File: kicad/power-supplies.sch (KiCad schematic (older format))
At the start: 22 parts, among them U3 MCP1603, U4 MIC2776L, U5 MIC5501-XYM5

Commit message: Finished initial part selection, built footprints
I'm not sure about my footprint selection for the expansion headers,
even though it is just a 0.1" header I want to be fairly exact about the
length the pins stick out and how close the female header is to the
edge, so that I can get a good distance between the two boards.
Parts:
- C14, C18: footprint (none) -> Capacitors_SMD:C_0805; Part No. (none) -> 1276-6464-1-ND
- C15, C17, C20, C21: footprint (none) -> Capacitors_SMD:C_0603; Part No. (none) -> 1276-6524-1-ND
- C16, C19: footprint (none) -> Capacitors_SMD:C_0402; Part No. (none) -> 1276-1043-1-ND
- L2: footprint (none) -> midi-fader:Wurth_TPC_3816; Part No. (none) -> 732-1008-1-ND
- R14: footprint (none) -> Resistors_SMD:R_0805
- R15, R16, R18, R19, R20, R21, R22, R23: footprint (none) -> Resistors_SMD:R_0402
- U3: footprint (none) -> TO_SOT_Packages_SMD:TSOT-23-5
- U4, U5: footprint (none) -> TO_SOT_Packages_SMD:SOT-23-5
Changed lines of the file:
@@
 LIBS:valves
 LIBS:midi-fader
+LIBS:midi-fader-cache
 EELAYER 25 0
 EELAYER END
@@
 F 0 "U3" H 7450 2050 60  0000 C CNN
 F 1 "MCP1603" H 7300 2550 60  0000 C CNN
-F 2 "" H 7300 1900 60  0001 C CNN
+F 2 "TO_SOT_Packages_SMD:TSOT-23-5" H 7300 1900 60  0001 C CNN
 F 3 "" H 7300 1900 60  0001 C CNN
 F 4 "MCP1603T-330I/OSCT-ND" H 7300 2650 60  0001 C CNN "Part No."
@@
 F 0 "U5" H 3100 3650 60  0000 C CNN
 F 1 "MIC5501-XYM5" H 2900 4150 60  0000 C CNN
-F 2 "" H 2900 3800 60  0001 C CNN
+F 2 "TO_SOT_Packages_SMD:SOT-23-5" H 2900 3800 60  0001 C CNN
 F 3 "" H 2900 3800 60  0001 C CNN
 F 4 "576-4764-1-ND" H 2900 4250 60  0001 C CNN "Part No."
@@
 F 0 "L2" V 8100 2200 50  0000 C CNN
 F 1 "4.7u" V 8225 2200 50  0000 C CNN
-F 2 "" H 8150 2200 50  0001 C CNN
+F 2 "midi-fader:Wurth_TPC_3816" H 8150 2200 50  0001 C CNN
 F 3 "" H 8150 2200 50  0001 C CNN
+F 4 "732-1008-1-ND" H 8150 2200 60  0001 C CNN "Part No."
 	1    8150 2200
 	0    -1   -1   0
@@
 F 0 "C18" H 8975 2750 50  0000 L CNN
 F 1 "4.7u" H 8975 2550 50  0000 L CNN
-F 2 "" H 8988 2500 50  0001 C CNN
+F 2 "Capacitors_SMD:C_0805" H 8988 2500 50  0001 C CNN
 F 3 "" H 8950 2650 50  0001 C CNN
+F 4 "1276-6464-1-ND" H 8950 2650 60  0001 C CNN "Part No."
 	1    8950 2650
 	1    0    0    -1
 $EndComp
 $Comp
-L VBUS #PWR15
+L VBUS #PWR023
 U 1 1 5B3CF911
 P 1000 2100
-F 0 "#PWR15" H 1000 1950 50  0001 C CNN
+F 0 "#PWR023" H 1000 1950 50  0001 C CNN
 F 1 "VBUS" H 1000 2250 50  0000 C CNN
 F 2 "" H 1000 2100 50  0001 C CNN
@@
 F 0 "C14" H 1025 2550 50  0000 L CNN
 F 1 "4.7u" H 1025 2350 50  0000 L CNN
-F 2 "" H 1038 2300 50  0001 C CNN
+F 2 "Capacitors_SMD:C_0805" H 1038 2300 50  0001 C CNN
 F 3 "" H 1000 2450 50  0001 C CNN
+F 4 "1276-6464-1-ND" H 1000 2450 60  0001 C CNN "Part No."
 	1    1000 2450
 	1    0    0    -1
@@
 F 0 "C15" H 1325 2550 50  0000 L CNN
 F 1 "1u" H 1325 2350 50  0000 L CNN
-F 2 "" H 1338 2300 50  0001 C CNN
+F 2 "Capacitors_SMD:C_0603" H 1338 2300 50  0001 C CNN
 F 3 "" H 1300 2450 50  0001 C CNN
+F 4 "1276-6524-1-ND" H 1300 2450 60  0001 C CNN "Part No."
 	1    1300 2450
 	1    0    0    -1
@@
 F 0 "R15" V 2980 2450 50  0000 C CNN
 F 1 "10K" V 2900 2450 50  0000 C CNN
-F 2 "" V 2830 2450 50  0001 C CNN
+F 2 "Resistors_SMD:R_0402" V 2830 2450 50  0001 C CNN
 F 3 "" H 2900 2450 50  0001 C CNN
 	1    2900 2450
@@
 F 0 "R18" V 2980 2950 50  0000 C CNN
 F 1 "750" V 2900 2950 50  0000 C CNN
-F 2 "" V 2830 2950 50  0001 C CNN
+F 2 "Resistors_SMD:R_0402" V 2830 2950 50  0001 C CNN
 F 3 "" H 2900 2950 50  0001 C CNN
 	1    2900 2950
@@
 F 0 "R20" V 1980 3750 50  0000 C CNN
 F 1 "0" V 1900 3750 50  0000 C CNN
-F 2 "" V 1830 3750 50  0001 C CNN
+F 2 "Resistors_SMD:R_0402" V 1830 3750 50  0001 C CNN
 F 3 "" H 1900 3750 50  0001 C CNN
 	1    1900 3750
@@
 F 0 "R22" V 1980 4250 50  0000 C CNN
 F 1 "SPR" V 1900 4250 50  0000 C CNN
-F 2 "" V 1830 4250 50  0001 C CNN
+F 2 "Resistors_SMD:R_0402" V 1830 4250 50  0001 C CNN
 F 3 "" H 1900 4250 50  0001 C CNN
 	1    1900 4250
@@
 $EndComp
 $Comp
-L GND #PWR26
+L GND #PWR024
 U 1 1 5B3CFC0A
 P 1900 4600
-F 0 "#PWR26" H 1900 4350 50  0001 C CNN
+F 0 "#PWR024" H 1900 4350 50  0001 C CNN
 F 1 "GND" H 1900 4450 50  0000 C CNN
 F 2 "" H 1900 4600 50  0001 C CNN
@@
 F 0 "R14" V 1680 2450 50  0000 C CNN
 F 1 "1K" V 1600 2450 50  0000 C CNN
-F 2 "" V 1530 2450 50  0001 C CNN
+F 2 "Resistors_SMD:R_0805" V 1530 2450 50  0001 C CNN
 F 3 "" H 1600 2450 50  0001 C CNN
 	1    1600 2450
@@
 F 0 "U4" H 5650 2550 60  0000 C CNN
 F 1 "MIC2776L" H 5500 3050 60  0000 C CNN
-F 2 "" H 5500 2800 60  0001 C CNN
+F 2 "TO_SOT_Packages_SMD:SOT-23-5" H 5500 2800 60  0001 C CNN
 F 3 "" H 5500 2800 60  0001 C CNN
 F 4 "576-2686-1-ND" H 5500 3150 60  0001 C CNN "Part No."
@@
 $EndComp
 $Comp
-L GND #PWR18
+L GND #PWR025
 U 1 1 5B3D0BA6
 P 1000 2800
-F 0 "#PWR18" H 1000 2550 50  0001 C CNN
+F 0 "#PWR025" H 1000 2550 50  0001 C CNN
 F 1 "GND" H 1000 2650 50  0000 C CNN
 F 2 "" H 1000 2800 50  0001 C CNN
@@
 F 0 "C20" H 3575 4250 50  0000 L CNN
 F 1 "1u" H 3575 4050 50  0000 L CNN
-F 2 "" H 3588 4000 50  0001 C CNN
+F 2 "Capacitors_SMD:C_0603" H 3588 4000 50  0001 C CNN
 F 3 "" H 3550 4150 50  0001 C CNN
+F 4 "1276-6524-1-ND" H 3550 4150 60  0001 C CNN "Part No."
 	1    3550 4150
 	1    0    0    -1
@@
 F 0 "C21" H 3825 4250 50  0000 L CNN
 F 1 "1u" H 3825 4050 50  0000 L CNN
-F 2 "" H 3838 4000 50  0001 C CNN
+F 2 "Capacitors_SMD:C_0603" H 3838 4000 50  0001 C CNN
 F 3 "" H 3800 4150 50  0001 C CNN
+F 4 "1276-6524-1-ND" H 3800 4150 60  0001 C CNN "Part No."
 	1    3800 4150
 	1    0    0    -1
@@
 F 0 "C19" H 4525 3000 50  0000 L CNN
 F 1 "0.1u" H 4525 2800 50  0000 L CNN
-F 2 "" H 4538 2750 50  0001 C CNN
+F 2 "Capacitors_SMD:C_0402" H 4538 2750 50  0001 C CNN
 F 3 "" H 4500 2900 50  0001 C CNN
+F 4 "1276-1043-1-ND" H 4500 2900 60  0001 C CNN "Part No."
 	1    4500 2900
 	1    0    0    -1
 $EndComp
 $Comp
-L GND #PWR21
+L GND #PWR026
 U 1 1 5B3D1467
 P 4500 3150
-F 0 "#PWR21" H 4500 2900 50  0001 C CNN
+F 0 "#PWR026" H 4500 2900 50  0001 C CNN
 F 1 "GND" H 4500 3000 50  0000 C CNN
 F 2 "" H 4500 3150 50  0001 C CNN
@@
 F 0 "R21" V 4580 4050 50  0000 C CNN
 F 1 "10K" V 4500 4050 50  0000 C CNN
-F 2 "" V 4430 4050 50  0001 C CNN
+F 2 "Resistors_SMD:R_0402" V 4430 4050 50  0001 C CNN
 F 3 "" H 4500 4050 50  0001 C CNN
 	1    4500 4050
@@
 F 0 "R23" V 4580 4550 50  0000 C CNN
 F 1 "SPR" V 4500 4550 50  0000 C CNN
-F 2 "" V 4430 4550 50  0001 C CNN
+F 2 "Resistors_SMD:R_0402" V 4430 4550 50  0001 C CNN
 F 3 "" H 4500 4550 50  0001 C CNN
 	1    4500 4550
@@
 $EndComp
 $Comp
-L VDDA #PWR25
+L VDDA #PWR027
 U 1 1 5B3D1EBD
 P 3900 3700
-F 0 "#PWR25" H 3900 3550 50  0001 C CNN
+F 0 "#PWR027" H 3900 3550 50  0001 C CNN
 F 1 "VDDA" H 3900 3850 50  0000 C CNN
 F 2 "" H 3900 3700 50  0001 C CNN
@@
 $EndComp
 $Comp
-L GND #PWR27
+L GND #PWR028
 U 1 1 5B3D212E
 P 4500 4800
-F 0 "#PWR27" H 4500 4550 50  0001 C CNN
+F 0 "#PWR028" H 4500 4550 50  0001 C CNN
 F 1 "GND" H 4500 4650 50  0000 C CNN
 F 2 "" H 4500 4800 50  0001 C CNN
@@
 $EndComp
 $Comp
-L GND #PWR22
+L GND #PWR029
 U 1 1 5B3D21E1
 P 2900 3200
-F 0 "#PWR22" H 2900 2950 50  0001 C CNN
+F 0 "#PWR029" H 2900 2950 50  0001 C CNN
 F 1 "GND" H 2900 3050 50  0000 C CNN
 F 2 "" H 2900 3200 50  0001 C CNN
@@
 $EndComp
 $Comp
-L GND #PWR23
+L GND #PWR030
 U 1 1 5B3D2387
 P 5500 3200
-F 0 "#PWR23" H 5500 2950 50  0001 C CNN
+F 0 "#PWR030" H 5500 2950 50  0001 C CNN
 F 1 "GND" H 5500 3050 50  0000 C CNN
 F 2 "" H 5500 3200 50  0001 C CNN
@@
 F 0 "C16" H 8475 2750 50  0000 L CNN
 F 1 "0.1u" H 8475 2550 50  0000 L CNN
-F 2 "" H 8488 2500 50  0001 C CNN
+F 2 "Capacitors_SMD:C_0402" H 8488 2500 50  0001 C CNN
 F 3 "" H 8450 2650 50  0001 C CNN
+F 4 "1276-1043-1-ND" H 8450 2650 60  0001 C CNN "Part No."
 	1    8450 2650
 	1    0    0    -1
@@
 F 0 "C17" H 8725 2750 50  0000 L CNN
 F 1 "1u" H 8725 2550 50  0000 L CNN
-F 2 "" H 8738 2500 50  0001 C CNN
+F 2 "Capacitors_SMD:C_0603" H 8738 2500 50  0001 C CNN
 F 3 "" H 8700 2650 50  0001 C CNN
+F 4 "1276-6524-1-ND" H 8700 2650 60  0001 C CNN "Part No."
 	1    8700 2650
 	1    0    0    -1
@@
 15mA\n50mW\nRC=1.47ms
 $Comp
-L GND #PWR20
+L GND #PWR031
 U 1 1 5B3D2E2E
 P 8450 3000
-F 0 "#PWR20" H 8450 2750 50  0001 C CNN
+F 0 "#PWR031" H 8450 2750 50  0001 C CNN
 F 1 "GND" H 8450 2850 50  0000 C CNN
 F 2 "" H 8450 3000 50  0001 C CNN
@@
 F 0 "R16" V 6480 2450 50  0000 C CNN
 F 1 "SPR" V 6400 2450 50  0000 C CNN
-F 2 "" V 6330 2450 50  0001 C CNN
+F 2 "Resistors_SMD:R_0402" V 6330 2450 50  0001 C CNN
 F 3 "" H 6400 2450 50  0001 C CNN
 	1    6400 2450
@@
 F 0 "R19" V 6480 3050 50  0000 C CNN
 F 1 "SPR" V 6400 3050 50  0000 C CNN
-F 2 "" V 6330 3050 50  0001 C CNN
+F 2 "Resistors_SMD:R_0402" V 6330 3050 50  0001 C CNN
 F 3 "" H 6400 3050 50  0001 C CNN
 	1    6400 3050
@@
 $EndComp
 $Comp
-L GND #PWR24
+L GND #PWR032
 U 1 1 5B3D365C
 P 6400 3300
-F 0 "#PWR24" H 6400 3050 50  0001 C CNN
+F 0 "#PWR032" H 6400 3050 50  0001 C CNN
 F 1 "GND" H 6400 3150 50  0000 C CNN
 F 2 "" H 6400 3300 50  0001 C CNN
@@
 $EndComp
 $Comp
-L VDD #PWR16
+L VDD #PWR033
 U 1 1 5B3D3EA7
 P 9300 2100
-F 0 "#PWR16" H 9300 1950 50  0001 C CNN
+F 0 "#PWR033" H 9300 1950 50  0001 C CNN
 F 1 "VDD" H 9300 2250 50  0000 C CNN
 F 2 "" H 9300 2100 50  0001 C CNN
@@
 	1900 4400 1900 4600
 $Comp
-L GND #PWR19
+L GND #PWR034
 U 1 1 5B3D4CA8
 P 7300 2800
-F 0 "#PWR19" H 7300 2550 50  0001 C CNN
+F 0 "#PWR034" H 7300 2550 50  0001 C CNN
 F 1 "GND" H 7300 2650 50  0000 C CNN
 F 2 "" H 7300 2800 50  0001 C CNN
@@
 Vth=4.3V
 $Comp
-L VDDA #PWR17
+L VDDA #PWR035
 U 1 1 5B3D5A35
 P 4500 2600
-F 0 "#PWR17" H 4500 2450 50  0001 C CNN
+F 0 "#PWR035" H 4500 2450 50  0001 C CNN
 F 1 "VDDA" H 4500 2750 50  0000 C CNN
 F 2 "" H 4500 2600 50  0001 C CNN

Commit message: Completed initial placement
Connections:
- net ~VDD_SHDN: now reaches R16.2, R19.1, U3.3 (~SHDN), U4.1 (~RST)
- net VDD_L: now reaches L2.1, U3.5 (Lx)
- net VDDA_EN: now reaches R20.2, R22.1, U5.3 (EN)
- net VDD_EN_SENSE: now reaches R15.2, R18.1, U4.4 (IN)
- net VDD_EN_MR: now reaches R21.2, R23.1, U4.3 (~MR)
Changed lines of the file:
@@
 $EndComp
 Connection ~ 4500 2700
+Text Label 3600 2700 0    60   ~ 0
+VDD_EN_SENSE
+Text Label 4550 4300 0    60   ~ 0
+VDD_EN_MR
+Text Label 5950 2800 0    60   ~ 0
+~VDD_SHDN
+Text Label 7850 2200 0    60   ~ 0
+VDD_L
+Text Label 2000 4000 0    60   ~ 0
+VDDA_EN
 $EndSCHEMATC

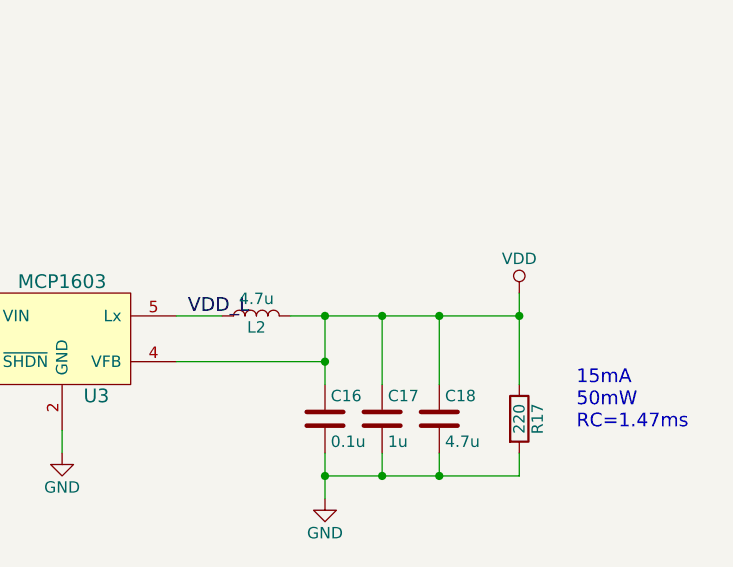
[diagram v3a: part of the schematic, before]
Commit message: Created shift register circuitry and imported footprints
I think 5MHz to 10MHz is the theoretical maximum of this circuit. Actual
frequency will probably be around 5MHz or somewhat less given the signal
integrity issues on a 2-layer board with this many plane breaks.

Created footprints for button and HTSSOP

The HTSSOP footprint is special because I plan to hand solder, so I
added excessive thermal vias and a bare pad on the backside.

The netlist is imported to the PCB, but only the switches are placed.
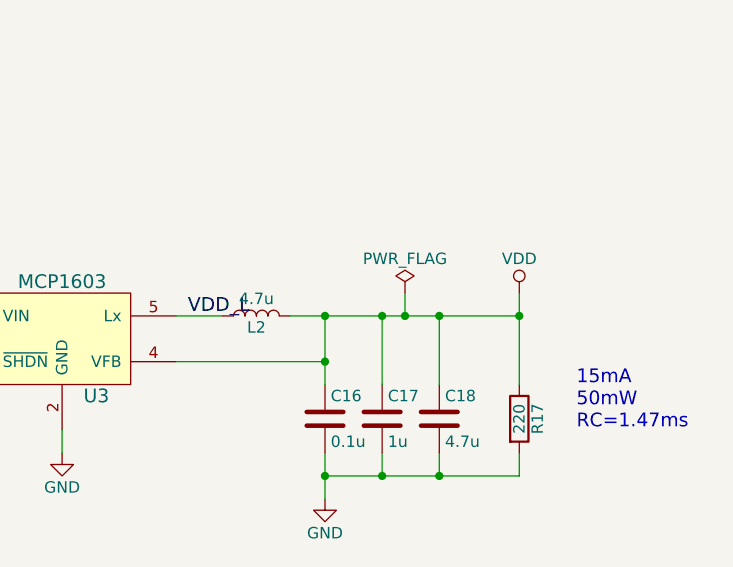
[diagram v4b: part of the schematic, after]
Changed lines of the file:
@@
 Text Label 2000 4000 0    60   ~ 0
 VDDA_EN
+$Comp
+L PWR_FLAG #FLG024
+U 1 1 5B41D3F3
+P 8800 2100
+F 0 "#FLG024" H 8800 2175 50  0001 C CNN
+F 1 "PWR_FLAG" H 8800 2250 50  0000 C CNN
+F 2 "" H 8800 2100 50  0001 C CNN
+F 3 "" H 8800 2100 50  0001 C CNN
+	1    8800 2100
+	1    0    0    -1
+$EndComp
+Wire Wire Line
+	8800 2100 8800 2200
+Connection ~ 8800 2200
 $EndSCHEMATC

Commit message: Added stub-removal resistors on clock lines, started cleaning silkscreen
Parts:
- C15, C17, C20, C21: Part No. 1276-6524-1-ND -> 1276-1182-1-ND
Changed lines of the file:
@@
 F 2 "Capacitors_SMD:C_0603" H 1338 2300 50  0001 C CNN
 F 3 "" H 1300 2450 50  0001 C CNN
-F 4 "1276-6524-1-ND" H 1300 2450 60  0001 C CNN "Part No."
+F 4 "1276-1182-1-ND" H 1300 2450 60  0001 C CNN "Part No."
 	1    1300 2450
 	1    0    0    -1
@@
 F 2 "Capacitors_SMD:C_0603" H 3588 4000 50  0001 C CNN
 F 3 "" H 3550 4150 50  0001 C CNN
-F 4 "1276-6524-1-ND" H 3550 4150 60  0001 C CNN "Part No."
+F 4 "1276-1182-1-ND" H 3550 4150 60  0001 C CNN "Part No."
 	1    3550 4150
 	1    0    0    -1
@@
 F 2 "Capacitors_SMD:C_0603" H 3838 4000 50  0001 C CNN
 F 3 "" H 3800 4150 50  0001 C CNN
-F 4 "1276-6524-1-ND" H 3800 4150 60  0001 C CNN "Part No."
+F 4 "1276-1182-1-ND" H 3800 4150 60  0001 C CNN "Part No."
 	1    3800 4150
 	1    0    0    -1
@@
 F 2 "Capacitors_SMD:C_0603" H 8738 2500 50  0001 C CNN
 F 3 "" H 8700 2650 50  0001 C CNN
-F 4 "1276-6524-1-ND" H 8700 2650 60  0001 C CNN "Part No."
+F 4 "1276-1182-1-ND" H 8700 2650 60  0001 C CNN "Part No."
 	1    8700 2650
 	1    0    0    -1
